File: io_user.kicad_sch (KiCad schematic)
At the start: 49 parts, among them J15 TSOP31338, J18 TSW-101-08-T-T-RA, J19 TSW-101-08-T-T-RA, J20 TSW-101-08-T-T-RA, J21 0470531000, J5 503182-1852, J8 30310-5002HB, Q4 BC847, Q5 BC847, Q6 BC847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

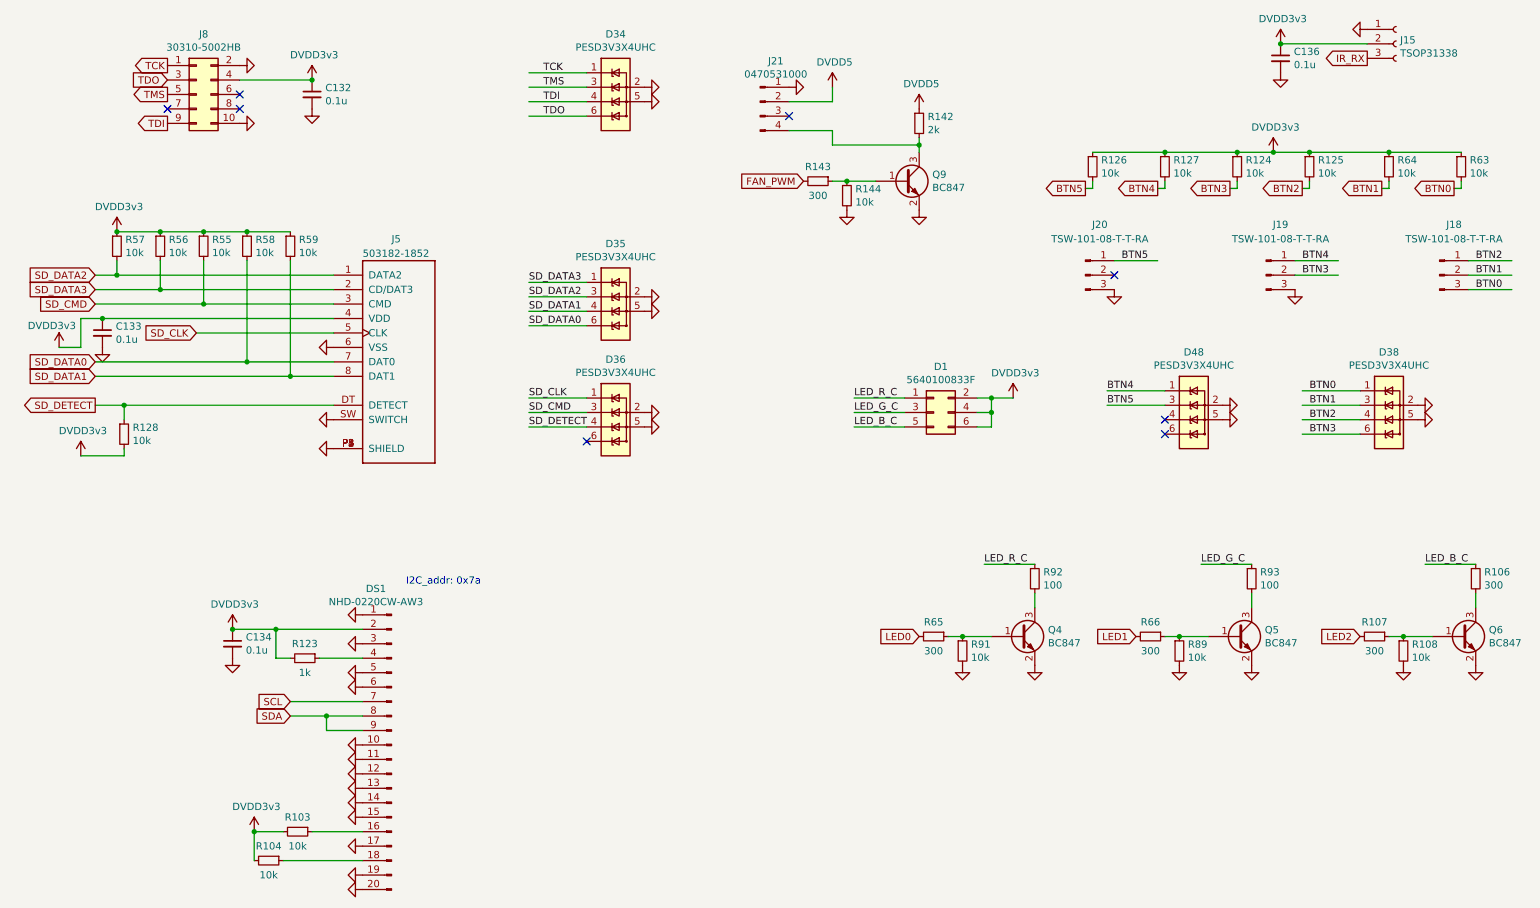
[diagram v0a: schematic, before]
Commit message: update schematic to v1.5
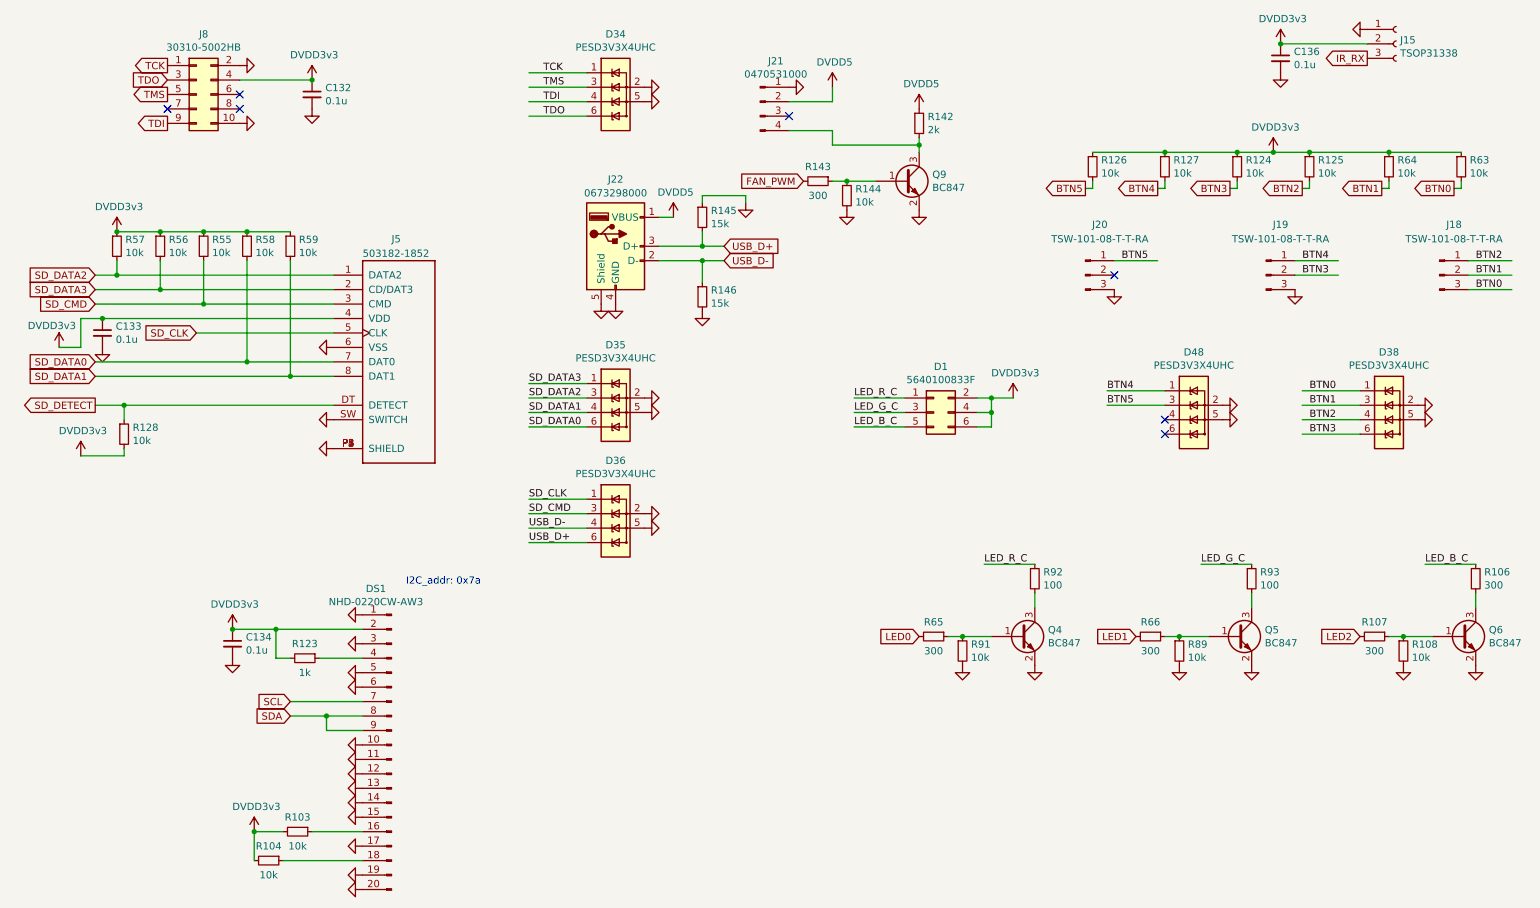
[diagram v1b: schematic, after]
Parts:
- added J22: 0673298000, custom_components:USB_A_Molex_067329-8000, symbol Connector:USB_A
- added R145, R146: 15k, Resistor_SMD:R_0402_1005Metric, symbol Device:R_Small
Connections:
- net DVDD5: now also J22.1 (VBUS)
- net GND: now also J22.4 (GND), J22.5 (Shield), R145.1, R146.2
- net SD_DETECT: no longer D36.4 (IO3)
- net USB_D+: now reaches D36.6 (IO4)
- net USB_D+: now also J22.3 (D+), R145.2
- new net USB_D-: D36.4 (IO3), J22.2 (D-), R146.1
- no-connect marks 8 -> 7
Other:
- moved on the sheet: D35, D36

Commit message: update schematic to v1.6
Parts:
- J21: footprint Connector_PinHeader_2.54mm:PinHeader_1x04_P2.54mm_Vertical -> Connector:FanPinHeader_1x04_P2.54mm_Vertical
